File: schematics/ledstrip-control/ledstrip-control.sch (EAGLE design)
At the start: 13 parts, among them IC1 LD1117S33CTR, Q3 IRF9530, U1 PHOTON_WITH_HEADERS

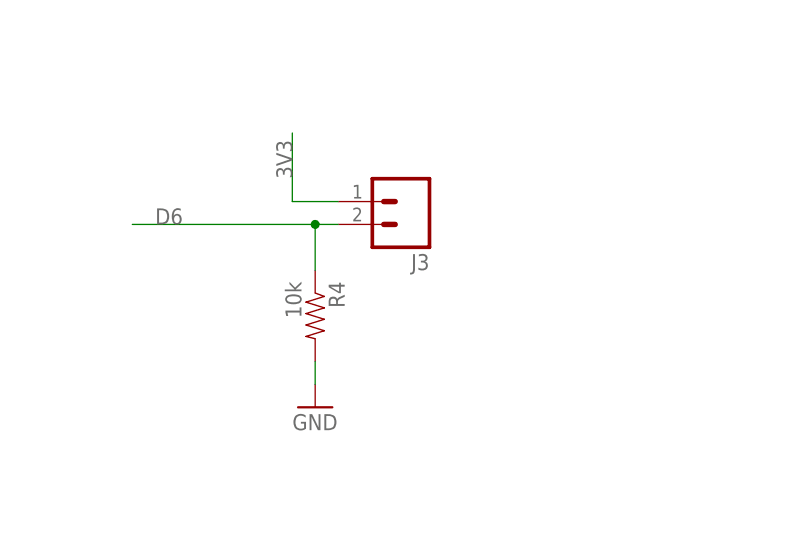
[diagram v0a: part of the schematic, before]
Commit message: Prepared pcb design for ordering
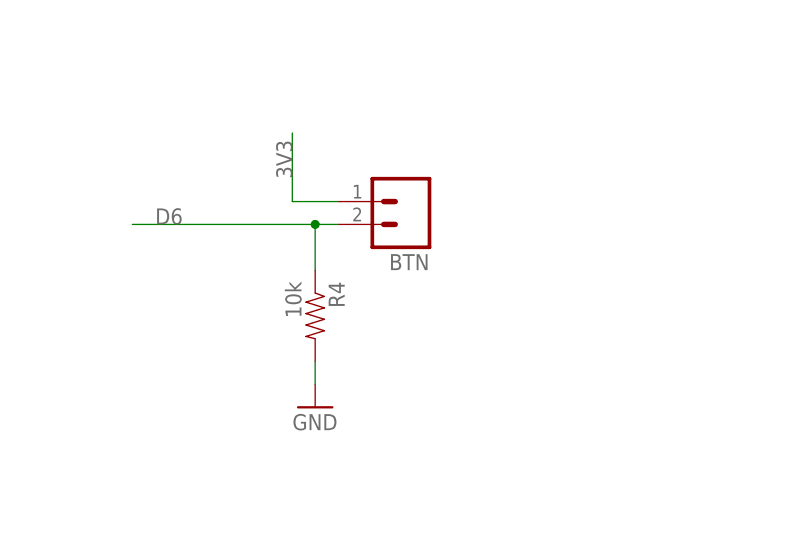
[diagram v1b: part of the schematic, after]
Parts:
- renumbered J3 to BTN
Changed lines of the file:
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@@
 <part name="C1" library="SparkFun-Passives" deviceset="CAP" device="PTH" value="100nF"/>
 <part name="GND9" library="SparkFun-Aesthetics" deviceset="GND" device=""/>
-<part name="J3" library="SparkFun-Connectors" deviceset="M02" device="PTH"/>
+<part name="BTN" library="SparkFun-Connectors" deviceset="M02" device="PTH"/>
 <part name="R4" library="SparkFun-Passives" deviceset="RESISTOR" device="AXIAL-0.3" value="10k"/>
 <part name="GND10" library="SparkFun-Aesthetics" deviceset="GND" device=""/>
@@
 <instance part="C1" gate="G$1" x="53.34" y="137.16"/>
 <instance part="GND9" gate="1" x="53.34" y="127"/>
-<instance part="J3" gate="G$1" x="218.44" y="154.94" rot="R180"/>
+<instance part="BTN" gate="G$1" x="218.44" y="154.94" rot="R180"/>
 <instance part="R4" gate="G$1" x="208.28" y="142.24" rot="R270"/>
 <instance part="GND10" gate="1" x="208.28" y="132.08"/>
@@
 </segment>
 <segment>
-<pinref part="J3" gate="G$1" pin="1"/>
+<pinref part="BTN" gate="G$1" pin="1"/>
 <wire x1="210.82" y1="154.94" x2="205.74" y2="154.94" width="0.1524" layer="91"/>
 <wire x1="205.74" y1="154.94" x2="205.74" y2="162.56" width="0.1524" layer="91"/>
@@
 <net name="D6" class="0">
 <segment>
-<pinref part="J3" gate="G$1" pin="2"/>
+<pinref part="BTN" gate="G$1" pin="2"/>
 <wire x1="210.82" y1="152.4" x2="208.28" y2="152.4" width="0.1524" layer="91"/>
 <junction x="208.28" y="152.4"/>
